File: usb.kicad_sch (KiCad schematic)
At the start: 50 parts, among them J4 Conn_USB-C_WE_632723300011, Q10 PJE138K, Q11 PJE138K, U3 HD3SS3220RNH, U4 AP22615A_TSOT26, U5 TPD4E05U06QDQARQ1, U6 TPD4E05U06QDQARQ1, U7 TPD4E05U06QDQARQ1

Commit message: [#54474] Complete USB schematics
- merge sch usb&debug
- add USB/4xUART bridge
- add USB-PD managament
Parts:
- removed C22, C24, C25, C26, C27, C28, C29, C31: C_100n_0402, antmicro-footprints:C_0402_1005Metric, symbol antmicroCapacitors0402:C_100n_0402
- removed C23, C30: C_10u_0603, antmicro-footprints:C_0603_1608Metric, symbol antmicroCapacitors0603:C_10u_0603
- removed D8: ESD9X5.0ST5G, antmicro-footprints:SOD-923, symbol antmicroTVSDiodes:ESD9X5.0ST5G
- removed D9: LED_G_0603_LTST-C190GKT, antmicro-footprints:LED_0603_1608Metric_G, symbol antmicroLEDIndicationDiscrete:LED_G_0603_LTST-C190GKT
- removed J4: Conn_USB-C_WE_632723300011, antmicro-footprints:USB-C_Receptacle_WE_632723300011, symbol antmicroUSBConnectors:USB-C_WE_632723300011
- removed Q10, Q11: PJE138K, antmicro-footprints:SOT-523, symbol antmicroTransistorsFETsMOSFETsSingle:PJE138K
- removed R29, R30, R32, R33, R34, R35, R36, R37, R38, R39, R40, R53: R_0R_0402, antmicro-footprints:R_0402_1005Metric, symbol antmicroResistors0402:R_0R_0402
- removed R31, R41, R45, R47, R49, R50, R54, R55: R_10k_0402, antmicro-footprints:R_0402_1005Metric, symbol antmicroResistors0402:R_10k_0402
- removed R42, R43, R44, R56: R_200k_0402, antmicro-footprints:R_0402_1005Metric, symbol antmicroResistors0402:R_200k_0402
- removed R46: R_1k_0402, antmicro-footprints:R_0402_1005Metric, symbol antmicroResistors0402:R_1k_0402
- removed R48: R_887k_0402, antmicro-footprints:R_0402_1005Metric, symbol antmicroResistors0402:R_887k_0402
- removed R51: R_2k2_0402, antmicro-footprints:R_0402_1005Metric, symbol antmicroResistors0402:R_2k2_0402
- removed R52: R_470R_0402, antmicro-footprints:R_0402_1005Metric, symbol antmicroResistors0402:R_470R_0402
- removed TP6, TP7: TP_0.75mm_SMD, antmicro-footprints:TP_SMD_0.75mm, symbol antmicroTestPoints:TP_0.75mm_SMD
- removed U3: HD3SS3220RNH, antmicro-footprints:WQFN-30_1EP_4.6x2.6mm_P0.4mm, symbol antmicroInterfaceControllers:HD3SS3220RNH
- removed U4: AP22615A_TSOT26, antmicro-footprints:TSOT23-6, symbol antmicroPMICPowerDistributionSwitchesLoadDrivers:AP22615A_TSOT26
- removed U5, U6, U7: TPD4E05U06QDQARQ1, antmicro-footprints:USON-10_2.5x1mm_P0.5mm, symbol antmicroTVSDiodes:TPD4E05U06QDQARQ1
- added C? (x17): C_100n_0402, antmicro-footprints:C_0402_1005Metric, symbol antmicroCapacitors0402:C_100n_0402
- added C? (x2): C_18p_0402, antmicro-footprints:C_0402_1005Metric, symbol antmicroCapacitors0402:C_18p_0402
- added C? (x2): C_4u7_0402, antmicro-footprints:C_0402_1005Metric, symbol antmicroCapacitors0402:C_4u7_0402
- added C? (x2): C_100n_100V_0805, antmicro-footprints:C_0805_2012Metric, symbol antmicroCapacitorsmisc:C_100n_100V_0805
- added C? (x2): C_1u_0402, antmicro-footprints:C_0402_1005Metric, symbol antmicroCapacitors0402:C_1u_0402
- added C? (x2): C_1u_25V_0603, antmicro-footprints:C_0603_1608Metric, symbol antmicroCapacitors0603:C_1u_25V_0603
- added D? (x3): LED_G, antmicro-footprints:LED_0603_1608Metric_R, symbol antmicroLEDIndicationDiscrete:LED_R_0603_598-8D80-107F
- added D? (x2): ESDA25P35-1U1M, antmicro-footprints:ESDA25P35-1U1M, symbol antmicroTVSDiodes:ESDA25P35-1U1M
- added D? (x4): RB521S30T1G, antmicro-footprints:SOD-523, symbol antmicroDiodesRectifiersSingle:RB521S30T1G
- added D? (x2): PUSB3F96X_PASS, antmicro-footprints:Nexperia_DFN-10_2.5x1mm_P0.5mm, symbol antmicroTVSDiodes:PUSB3F96X_PASS
- added D?: LED_Y, antmicro-footprints:LED_0402_1005Metric_Y, symbol antmicroLEDIndicationDiscrete:LED_Y_0402_VLMY1500-GS08
- added FB? (x3): FB_120Z_1.3A_0402, antmicro-footprints:FB_0402_1005Metric, symbol antmicroFerriteBeadsandChips:FB_120Z_1.3A_Murata-BLM15PD_0402
- added J16, J4: USB-C_GCT_USB4105-GF-A, antmicro-footprints:USB-C_Receptacle_GCT_USB4105-GF-A, symbol antmicroUSBConnectors:USB-C_GCT_USB4105-GF-A
- added L? (x2): NFP0QHB242HS2D, antmicro-footprints:Choke_025020_0605Metric, symbol antmicroCommonModeChokes:Choke_NFP0QHB242HS2D
- added Q? (x4): PJE138K, antmicro-footprints:SOT-523, symbol antmicroTransistorsFETsMOSFETsSingle:PJE138K
- added Q? (x2): SQS401EN-T1_BE3, antmicro-footprints:Vishay_PowerPAK_1212-8_Single, symbol antmicroTransistorsFETsMOSFETsSingle:SQS401EN-T1_BE3
- added Q?: SSM3J332R, antmicro-footprints:SOT-23-3, symbol antmicroTransistorsFETsMOSFETsSingle:SSM3J332R
- added R? (x8): R_100k_0402, antmicro-footprints:R_0402_1005Metric, symbol antmicroResistors0402:R_100k_0402
- added R? (x3): R_1k_0402, antmicro-footprints:R_0402_1005Metric, symbol antmicroResistors0402:R_1k_0402
- added R?: R_470R_0402, antmicro-footprints:R_0402_1005Metric, symbol antmicroResistors0402:R_470R_0402
- added R? (x3): R_10k_0402, antmicro-footprints:R_0402_1005Metric, symbol antmicroResistors0402:R_10k_0402
- added R? (x2): R_15k_0603, antmicro-footprints:R_0603_1608Metric, symbol antmicroResistors0603:R_15k_0603
- added R? (x2): R_2k2_0402, antmicro-footprints:R_0402_1005Metric, symbol antmicroResistors0402:R_2k2_0402
- added R?: R_100R_0402, antmicro-footprints:R_0402_1005Metric, symbol antmicroResistors0402:R_100R_0402
- added R?: R_12k_0402, antmicro-footprints:R_0402_1005Metric, symbol antmicroResistors0402:R_12k_0402
- added TP? (x8): TP_0.75mm_SMD, antmicro-footprints:TP_SMD_0.75mm, symbol antmicroTestPoints:TP_0.75mm_SMD
- added U? (x2): NCP730BMT330_WSON, antmicro-footprints:WSON-6-1EP_2x2mm_P0.65mm, symbol antmicroPMICVoltageRegulatorsLinear:NCP730BMT330_WSON
- added U?: AP22615A_TSOT26, antmicro-footprints:TSOT23-6, symbol antmicroPMICPowerDistributionSwitchesLoadDrivers:AP22615A_TSOT26
- added U?: 93LC66BT_DFN, antmicro-footprints:DFN-8-1EP_3x2mm_P0.5mm_EP1.36x1.46mm, symbol antmicroMemory:93LC66BT_DFN
- added U?: FT4233HPQ, antmicro-footprints:QFN-76-1EP_9x9mm_P0.4mm_EP3.8x3.8mm, symbol antmicroInterfaceControllers:FT4233HPQ
- added Y?: Oscillator_SMD_12MHz_KX-7, antmicro-footprints:Oscillator_SMD_Geyer_KX-7-4Pin_3.2x2.5mm, symbol antmicroResonators:Resonator_12MHz_ABM8G
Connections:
- net +5V: now also C?.1, D?.2, R?.1, U?.6 (IN)
- net GND: now also C?.1, C?.1, C?.1, C?.2, C?.2, C?.2, C?.2, C?.2, C?.2, C?.2, C?.2, C?.2, C?.2, C?.2, C?.2, C?.2, C?.2, C?.2, C?.2, C?.2, C?.2, C?.2, C?.2, C?.2, C?.2, C?.2, C?.2, D?.1 (K), D?.1 (K), D?.2, D?.2, D?.3 (GND), D?.3 (GND), D?.8 (GND), D?.8 (GND), J16.A1 (GND), J16.A12 (GND), J16.B1 (GND), J16.B12 (GND), J16.SH, J4.A1 (GND), J4.A12 (GND), J4.B1 (GND), J4.B12 (GND), J4.SH, Q?.2 (S), Q?.2 (S), Q?.2 (S), Q?.2 (S), R?.1, R?.1, R?.2, R?.2, R?.2, R?.2, U?.11 (GND), U?.2 (GND), U?.3 (GND), U?.3 (GND), U?.3 (TEST), U?.31 (GND), U?.5 (GND), U?.55 (GND), U?.7 (GND), U?.7 (GND), U?.77 (GND), U?.9 (EP), Y?.2 (SH), Y?.4 (SH)
- new net: D?.1, R?.1 (x4)
- new net: D?.2, U?.75 (~{PWREN})
- new net: C?.1, U?.29 (OSCI), Y?.1
- new net: Q?.1 (G), Q?.3 (D), R?.2 (x2)
- new net: D?.1, D?.1, Q?.2 (S), R?.1, R?.1
- new net: Q?.3 (D), Q?.4 (G) (x2)
- new net: R?.1, R?.2, U?.4 (DO)
- new net: TP?.1, U?.46 (GPIO6)
- new net: C?.1, FB?.1, TP?.1, U?.1 (V_{OUT})
- new net: C?.1, D?.2, FB?.2
- new net: TP?.1, U?.58 (GPIO7)
- new net: R?.1, TP?.1, U?.4 (~{RESET})
- new net: R?.2, U?.5 (ISET)
- new net: C?.1, U?.30 (OSCO), Y?.3
- new net: Q?.1 (G), R?.1, R?.2
- new net: D?.2, U?.45 (~{SUSPEND})
- new net: R?.2, U?.65 (REF)
- new net AD_N: D?.5 (CH4), D?.6 (CH4), J4.A7 (D_{A}-), J4.B7 (D_{B}-), L?.1
- new net AD_P: D?.4 (CH3), D?.7 (CH3), J4.A6 (D_{A}+), J4.B6 (D_{B}+), L?.4
- new net DD_N: D?.5 (CH4), D?.6 (CH4), J16.A7 (D_{A}-), J16.B7 (D_{B}-), L?.1
- new net DD_P: D?.4 (CH3), D?.7 (CH3), J16.A6 (D_{A}+), J16.B6 (D_{B}+), L?.4
- new net EECLK: R?.2, U?.1 (EECLK), U?.2 (SCLK)
- new net EECS: R?.2, U?.1 (CS), U?.76 (EECS)
- new net EEDATA: R?.2, U?.2 (EEDATA), U?.3 (DI)
- new net FT4233.SCL: U?.60 (GPIO1)
- new net FT4233.SDA: U?.61 (GPIO0)
- new net IRQ: U?.59 (GPIO2)
- new net PD1_CC1: D?.1 (CH1), D?.10 (CH1), J4.A5 (CC_{1}), U?.70 (PD1_CC1)
- new net PD1_CC2: D?.2 (CH2), D?.9 (CH2), J4.B5 (CC_{2}), U?.67 (PD1_CC2)
- new net PD1_EN: Q?.1 (G), U?.5 (GPIO3)
- new net PD1_OUT_EN: U?.4 (EN), U?.7 (GPIO5)
- new net PD1_SVBUS: C?.1, R?.1, R?.2, TP?.1, U?.68 (PD1_SVBUS)
- new net PD2_CC1: D?.1 (CH1), D?.10 (CH1), J16.A5 (CC_{1}), U?.71 (PD2_CC1)
- new net PD2_CC2: D?.2 (CH2), D?.9 (CH2), J16.B5 (CC_{2}), U?.73 (PD2_CC2)
- new net PD2_EN: Q?.1 (G), U?.6 (GPIO4)
- new net PD2_SVBUS: C?.1, R?.1, R?.2, TP?.1, U?.72 (PD2_SVBUS)
- new net PROG_MODE: C?.1, R?.1, R?.2
- new net UART.0.RX: U?.9 (ADBUS1)
- new net UART.0.TX: U?.8 (ADBUS0)
- new net UART.1.RX: U?.20 (BDBUS1)
- new net UART.1.TX: U?.19 (BDBUS0)
- new net UART.2.RX: U?.37 (CDBUS1)
- new net UART.2.TX: U?.36 (CDBUS0)
- new net UART.3.RX: U?.49 (DDBUS1)
- new net UART.3.TX: U?.48 (DDBUS0)
- new net USBA.D_N: L?.2
- new net USBA.D_P: L?.3
- new net USBA_VBUS: C?.2, D?.2, D?.2 (A), J4.A4 (VBUS), J4.A9 (VBUS), J4.B4 (VBUS), J4.B9 (VBUS), Q?.5 (D), R?.1, R?.2, U?.1 (OUT)
- new net USBD.D_N: L?.2, U?.63 (DM)
- new net USBD.D_P: L?.3, U?.64 (DP)
- new net USBD_VBUS: C?.2, D?.2, D?.2 (A), J16.A4 (VBUS), J16.A9 (VBUS), J16.B4 (VBUS), J16.B9 (VBUS), Q?.5 (D), R?.1, R?.1, R?.2
- new net USB_1V2: C?.1, C?.1, C?.1, C?.1, C?.1, C?.1, TP?.1, U?.10 (VCORE), U?.27 (VCORE), U?.33 (VREGOUT), U?.47 (VCORE), U?.74 (VCORE)
- new net USB_3V3: C?.1, C?.1, C?.1, C?.1, C?.1, C?.1, C?.2, FB?.1, FB?.1, R?.1, R?.1, R?.1, R?.2, R?.2, R?.2, TP?.1, U?.1 (V_{OUT}), U?.12 (VCCIO), U?.28 (VCCIO), U?.41 (VCCIO), U?.54 (VCCIO), U?.8 (VCC)
- new net USB_VBUS: C?.1, C?.1, D?.1, Q?.3 (D), U?.4 (EN), U?.4 (EN), U?.6 (V_{IN}), U?.6 (V_{IN})
- new net VCC_PD: D?.1, U?.66 (VCC_PD), U?.69 (PD1_VCONN)
- new net VCC_USB: C?.1, FB?.2, U?.62 (VCC_USB)
- new net VREGIN: C?.1, FB?.2, U?.32 (VREGIN)
- new net V_{BUS}: Q?.1 (S), Q?.1 (S), Q?.2 (S), Q?.2 (S), Q?.3 (S), Q?.3 (S)
- no-connect marks 2 -> 34
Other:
- note added: "Decoupling and Filtering"
- note added: "EEPROM"
- note added: "ESD/EMI protection"
- note added: "FD4233 power selector"
- note added: "FT4233 supply"
- note added: "ISET = 3A"
- note added: "USB <-> 4x UART & PD controller"
- note added: "USB Application"
- note added: "USB Debug"
- note added: "USB-C VBUS voltage divider"
- note added: "USB-PD sink switches"
- note added: "USB-PD source switch"
- note added: "Use main 5V supply (if available) Otherwise use power from any USB port (5-20V) [USB power is used, only until main dcdc starts] [main 5V is preffered as results in higher LDO efficiency, in USB-PD scenario]"
- note removed: "10k - 3A 500k - 1.5A DNP - 900mA"
- note removed: "Both DNP - GPIO Mode HIGH - I2C Mode 0x67 LOW - I2C Mode 0x47"
- note removed: "Enable CC controller"
- note removed: "Enable MUX"
- note removed: "LOW: DFP role HIGH: NO ATTACH/UFP"
- note removed: "LOW: VCONN OC TRIP HIGH: NORMAL OPERATION"
- note removed: "Mode HIGH - DFP (HOST ONLY) LOW - UFP (DEVICE ONLY) DNP - DRP (DUAL ROLE PORT)"
- note removed: "NOTE: Populate 1/3"
- note removed: "TODO"
- note removed: "USB-C"
- note removed: "USBC1"

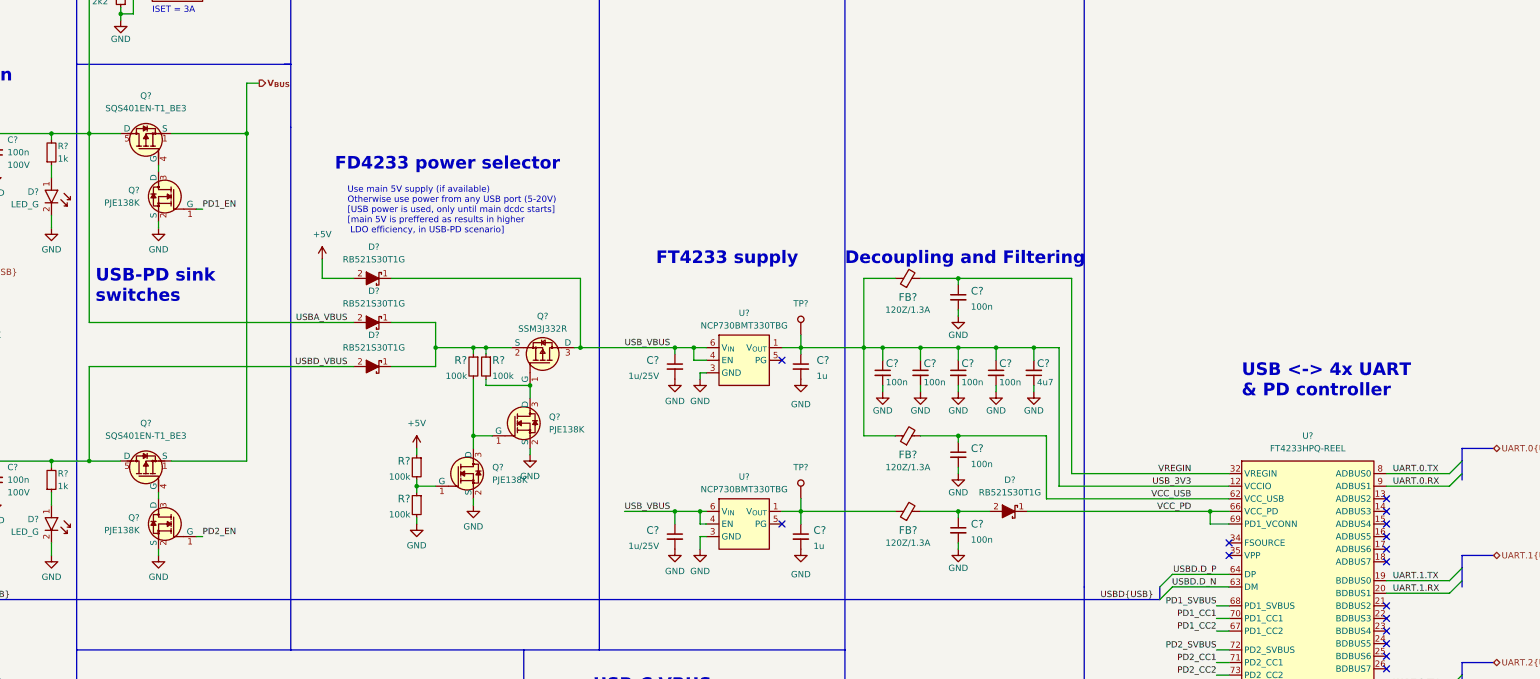
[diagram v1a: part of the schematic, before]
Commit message: [#54474] Fix USB VBUS switching
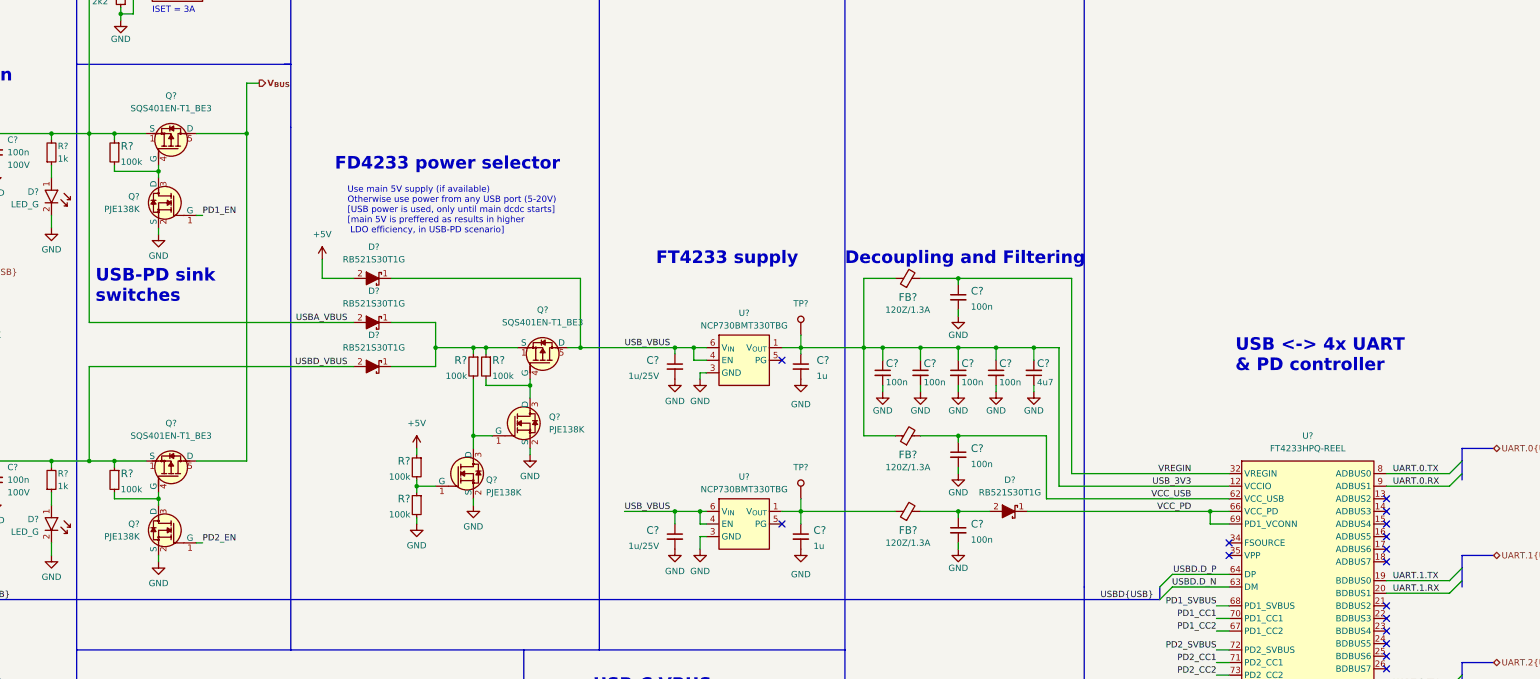
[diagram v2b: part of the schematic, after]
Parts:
- removed Q?: SSM3J332R, antmicro-footprints:SOT-23-3, symbol antmicroTransistorsFETsMOSFETsSingle:SSM3J332R
- added Q?: SQS401EN-T1_BE3, antmicro-footprints:Vishay_PowerPAK_1212-8_Single, symbol antmicroTransistorsFETsMOSFETsSingle:SQS401EN-T1_BE3
- added R? (x2): R_100k_0402, antmicro-footprints:R_0402_1005Metric, symbol antmicroResistors0402:R_100k_0402
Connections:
- net USBA_VBUS: now also Q?.1 (S), Q?.2 (S), Q?.3 (S), R?.1; no longer Q?.5 (D)
- net USBD_VBUS: now also Q?.1 (S), Q?.2 (S), Q?.3 (S), R?.1; no longer Q?.5 (D)
- net USB_VBUS: now also Q?.5 (D)
- net V_{BUS}: now also Q?.5 (D), Q?.5 (D); no longer Q?.1 (S), Q?.1 (S), Q?.2 (S), Q?.2 (S), Q?.3 (S), Q?.3 (S)
- net at Q?.3 (D), R?.2: now also Q?.4 (G)
- net at D?.1, D?.1, R?.1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: now also Q?.1 (S), Q?.2 (S), Q?.3 (S)
- net at Q?.3 (D), Q?.4 (G): now also R?.2 (x2)
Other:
- moved on the sheet: Q?

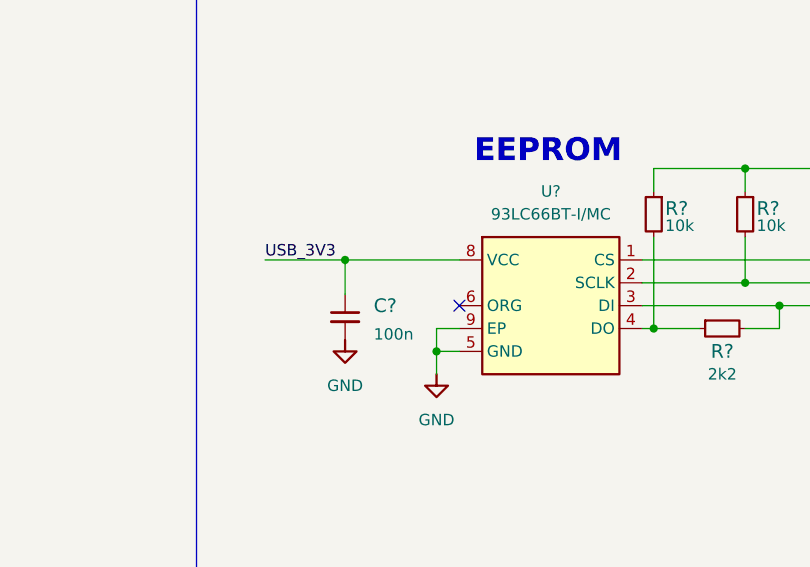
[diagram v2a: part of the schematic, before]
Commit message: [#54474] Tie EEPROM ORG pin to USB_3V3
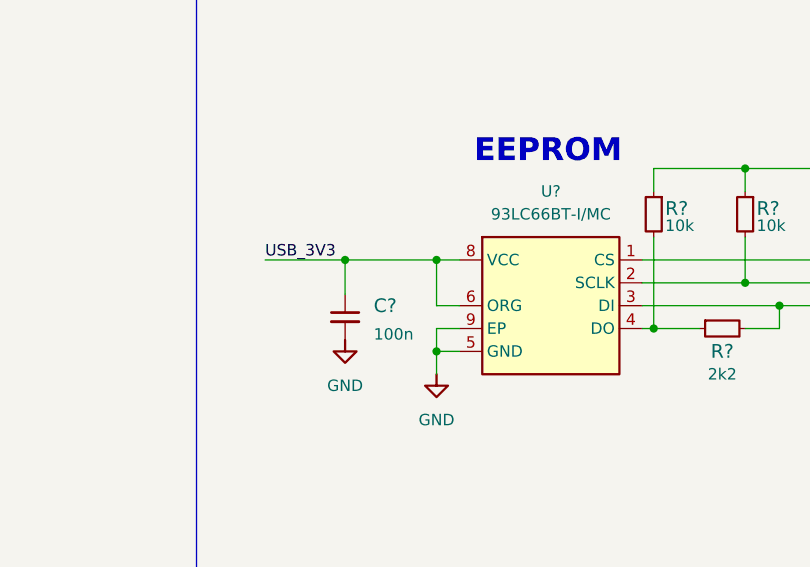
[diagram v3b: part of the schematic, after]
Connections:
- net USB_3V3: now also U?.6 (ORG)
- no-connect marks 34 -> 33
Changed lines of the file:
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@@
   (junction (at 328.93 218.44) (diameter 0) (color 0 0 0 0)
+  )
+  (junction (at 130.81 210.82) (diameter 0) (color 0 0 0 0)
   )
   (junction (at 250.19 110.49) (diameter 0) (color 0 0 0 0)
@@
   (no_connect (at 246.38 113.03))
   (no_connect (at 368.3 172.72))
-  (no_connect (at 133.35 215.9))
   (no_connect (at 368.3 191.77))
   (no_connect (at 368.3 196.85))
@@
     (stroke (width 0) (type default) (color 0 0 0 0))
   )
-  (wire (pts (xy 120.65 210.82) (xy 133.35 210.82))
+  (wire (pts (xy 120.65 210.82) (xy 130.81 210.82))
     (stroke (width 0) (type default) (color 0 0 0 0))
   )
@@
     (stroke (width 0) (type default) (color 0 0 0 0))
   )
+  (wire (pts (xy 130.81 215.9) (xy 130.81 210.82))
+    (stroke (width 0) (type default) (color 0 0 0 0))
+  )
   (wire (pts (xy 368.3 135.89) (xy 381 135.89))
     (stroke (width 0) (type default) (color 0 0 0 0))
@@
     (stroke (width 0) (type default) (color 0 0 0 0))
   )
+  (wire (pts (xy 130.81 210.82) (xy 133.35 210.82))
+    (stroke (width 0) (type default) (color 0 0 0 0))
+  )
   (wire (pts (xy 368.3 200.66) (xy 381 200.66))
     (stroke (width 0) (type default) (color 0 0 0 0))
@@
     (stroke (width 0) (type default) (color 0 0 0 0))
   )
+  (wire (pts (xy 133.35 215.9) (xy 130.81 215.9))
+    (stroke (width 0) (type default) (color 0 0 0 0))
+  )

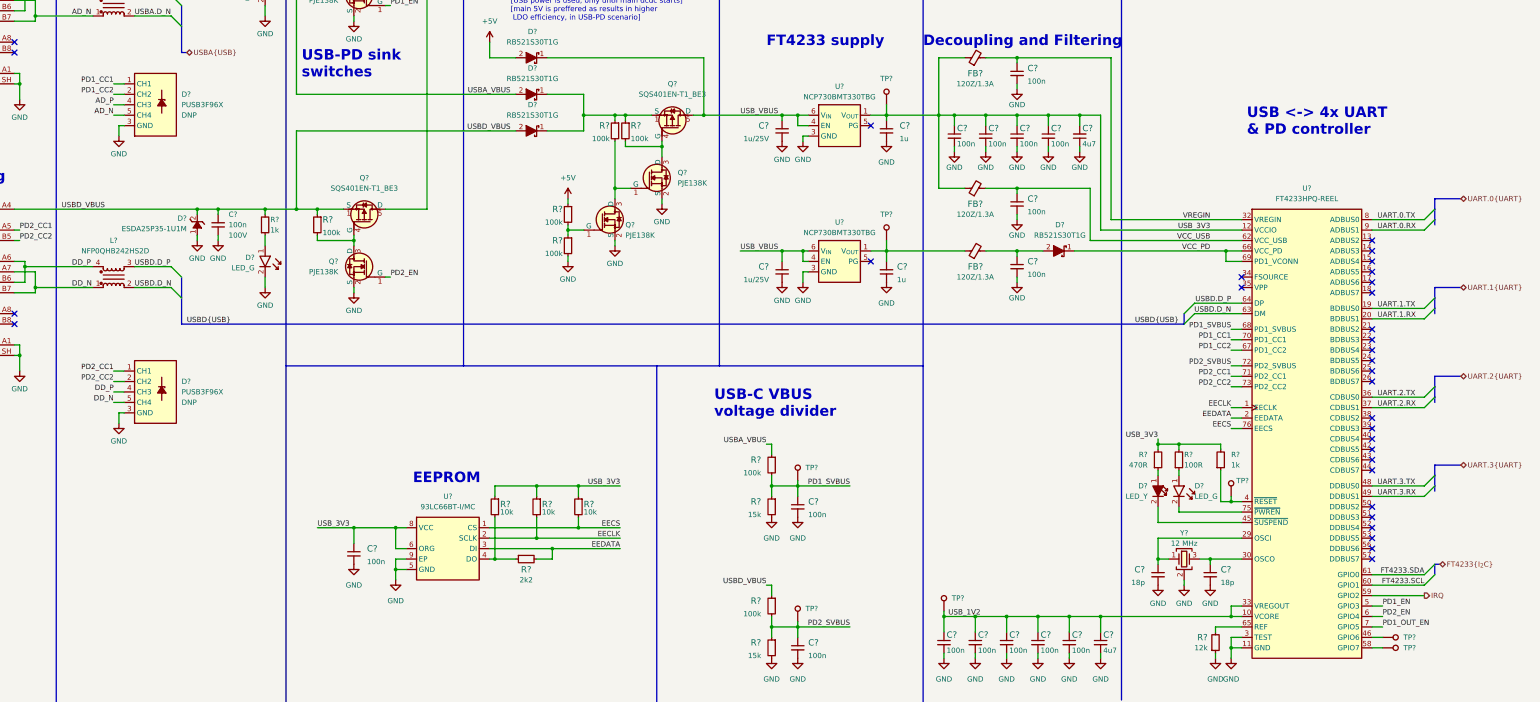
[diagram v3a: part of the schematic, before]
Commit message: [#54617] Clean labels: align & reduce duplicates
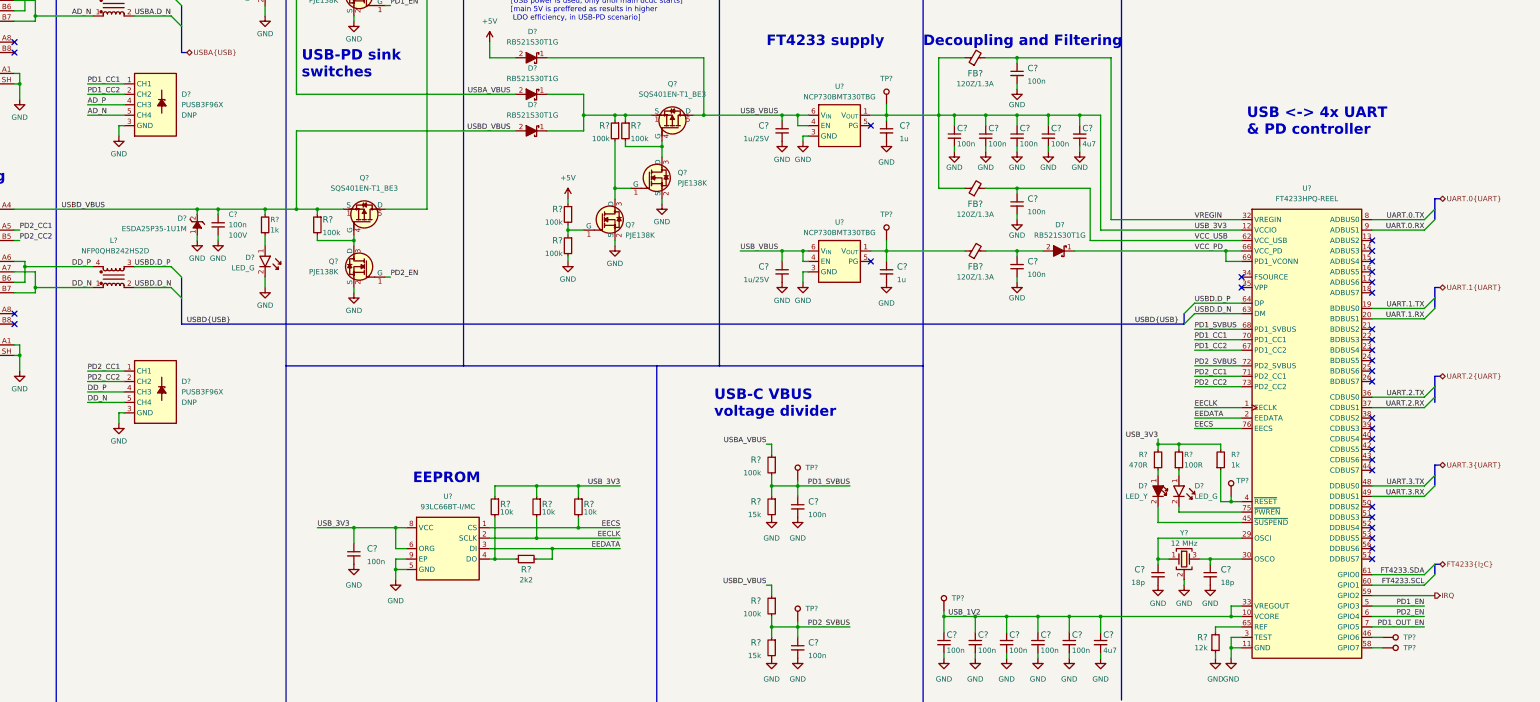
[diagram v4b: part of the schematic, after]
